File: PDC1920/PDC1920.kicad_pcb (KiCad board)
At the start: 2 copper layers, 113 x 16.8 mm, 20 parts, among them IC1 PIC16LF1826-I_SO, IC2 LM60CIM3_NOPB, J1 Conn_01x04, J2 Conn_01x06, J3 Conn_01x10_Male, U1 PressureSensor, U2 PressureSensor, U3 PressureSensor

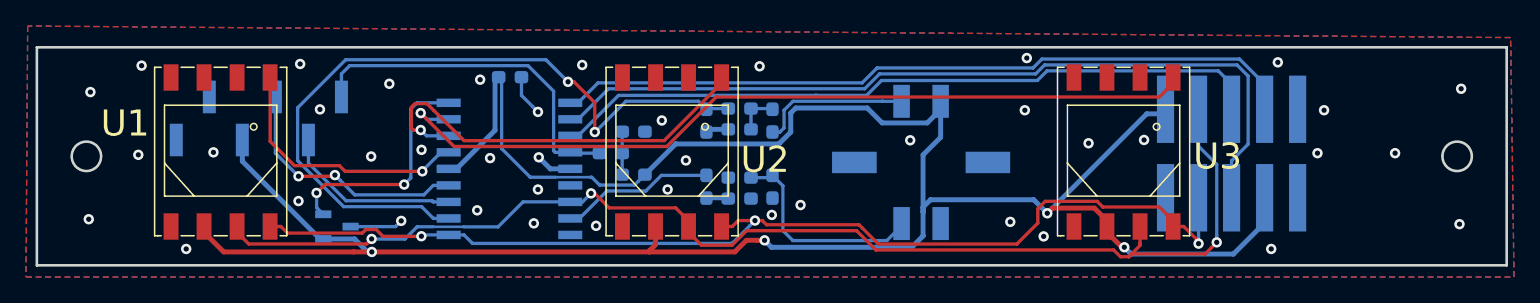
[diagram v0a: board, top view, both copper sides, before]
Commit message: Clearance changes
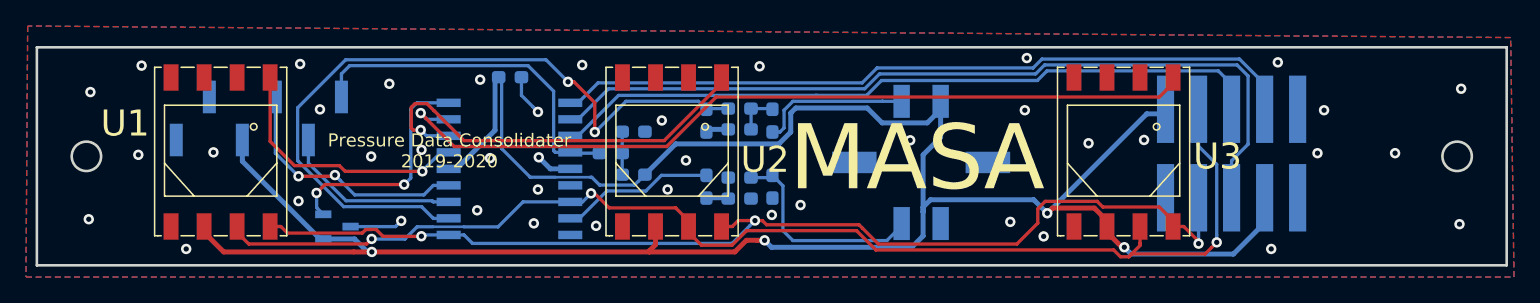
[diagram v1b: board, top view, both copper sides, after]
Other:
- board text added: "MASA"
- board text added: "Pressure Data Consolidater 2019-2020"
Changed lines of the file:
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@@
   (general
     (thickness 1.6)
-    (drawings 93)
+    (drawings 95)
     (tracks 374)
     (zones 0)
@@
       (psa4output false)
       (plotreference true)
-      (plotvalue true)
+      (plotvalue false)
       (plotinvisibletext false)
       (padsonsilk false)
@@
       (outputformat 1)
       (mirror false)
-      (drillshape 1)
+      (drillshape 0)
       (scaleselection 1)
-      (outputdirectory ""))
+      (outputdirectory "Gerber PDC/"))
   )
   (net 0 "")
@@
     )
   )
+  (gr_text MASA (at 118.0465 94.234) (layer F.SilkS)
+    (effects (font (size 5 5) (thickness 1)))
+  )
+  (gr_text "Pressure Data Consolidater\n2019-2020" (at 82.0928 93.6752) (layer F.SilkS)
+    (effects (font (size 1 1) (thickness 0.15)))
+  )
   (gr_line (start 163.3946 85.713125) (end 50.364601 85.713125) (layer Edge.Cuts) (width 0.2))
